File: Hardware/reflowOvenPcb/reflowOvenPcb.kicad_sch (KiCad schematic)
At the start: 0 parts

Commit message: PCB: started to add components
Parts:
- added U1: ATmega328P-A, Package_QFP:TQFP-32_7x7mm_P0.8mm, symbol MCU_Microchip_ATmega:ATmega328P-A
- added U2: MAX31856, Package_SO:TSSOP-14_4.4x5mm_P0.65mm, symbol Sensor_Temperature:MAX31856
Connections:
- new net: U1.21 (GND), U1.3 (GND), U1.5 (GND)
- new net: U1.4 (VCC), U1.6 (VCC)
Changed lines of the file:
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@@
 (kicad_sch (version 20230121) (generator eeschema)
   (paper "A4")
+  (symbol (lib_id "MCU_Microchip_ATmega:ATmega328P-A") (at 124.46 76.2 0) (unit 1)
+    (in_bom yes) (on_board yes) (dnp no) (fields_autoplaced)
+    (property "Reference" "U1" (at 126.4159 114.3 0)
+      (effects (font (size 1.27 1.27)) (justify left))
+    )
+    (property "Value" "ATmega328P-A" (at 126.4159 116.84 0)
+      (effects (font (size 1.27 1.27)) (justify left))
+    )
+    (property "Footprint" "Package_QFP:TQFP-32_7x7mm_P0.8mm" (at 124.46 76.2 0)
+      (effects (font (size 1.27 1.27) italic) hide)
+    )
+    (property "Datasheet" "http://ww1.microchip.com/downloads/en/DeviceDoc/ATmega328_P%20AVR%20MCU%20with%20picoPower%20Technology%20Data%20Sheet%2040001984A.pdf" (at 124.46 76.2 0)
+      (effects (font (size 1.27 1.27)) hide)
+    )
+    (pin "1")
+    (pin "10")
+    (pin "11")
+    (pin "12")
+    (pin "13")
+    (pin "14")
+    (pin "15")
+    (pin "16")
+    (pin "17")
+    (pin "18")
+    (pin "19")
+    (pin "2")
+    (pin "20")
+    (pin "21")
+    (pin "22")
+    (pin "23")
+    (pin "24")
+    (pin "25")
+    (pin "26")
+    (pin "27")
+    (pin "28")
+    (pin "29")
+    (pin "3")
+    (pin "30")
+    (pin "31")
+    (pin "32")
+    (pin "4")
+    (pin "5")
+    (pin "6")
+    (pin "7")
+    (pin "8")
+    (pin "9")
+    (instances
+      (project "reflowOvenPcb"
+        (path "/725b5e94-aab9-4b38-b207-68bd972bbc88"
+          (reference "U1") (unit 1)
+        )
+      )
+    )
+  )
+  (symbol (lib_id "Sensor_Temperature:MAX31856") (at 172.72 78.74 0) (unit 1)
+    (in_bom yes) (on_board yes) (dnp no) (fields_autoplaced)
+    (property "Reference" "U2" (at 177.2159 60.96 0)
+      (effects (font (size 1.27 1.27)) (justify left))
+    )
+    (property "Value" "MAX31856" (at 177.2159 63.5 0)
+      (effects (font (size 1.27 1.27)) (justify left))
+    )
+    (property "Footprint" "Package_SO:TSSOP-14_4.4x5mm_P0.65mm" (at 176.53 92.71 0)
+      (effects (font (size 1.27 1.27)) (justify left) hide)
+    )
+    (property "Datasheet" "https://datasheets.maximintegrated.com/en/ds/MAX31856.pdf" (at 171.45 73.66 0)
+      (effects (font (size 1.27 1.27)) hide)
+    )
+    (pin "1")
+    (pin "10")
+    (pin "11")
+    (pin "12")
+    (pin "13")
+    (pin "14")
+    (pin "2")
+    (pin "3")
+    (pin "4")
+    (pin "5")
+    (pin "6")
+    (pin "7")
+    (pin "8")
+    (pin "9")
+    (instances
+      (project "reflowOvenPcb"
+        (path "/725b5e94-aab9-4b38-b207-68bd972bbc88"
+          (reference "U2") (unit 1)
+        )
+      )
+    )
+  )
   (sheet_instances
     (path "/" (page "1"))

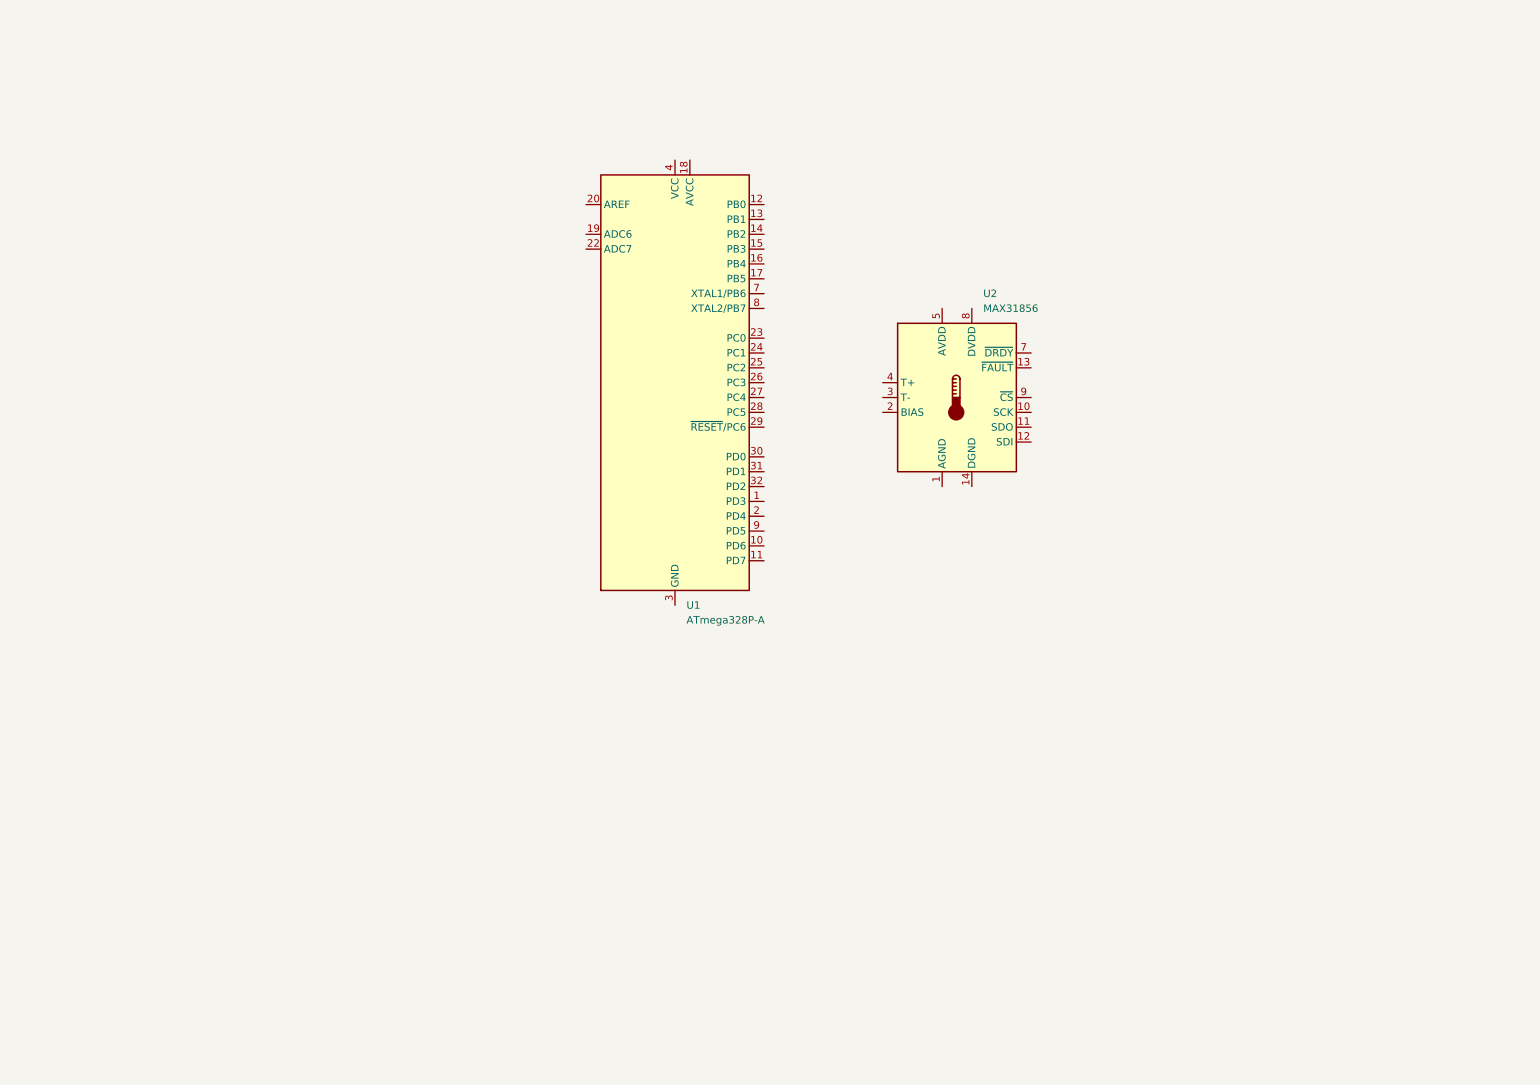
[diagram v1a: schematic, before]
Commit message: MCU wiring finished, added components to OLED SSD
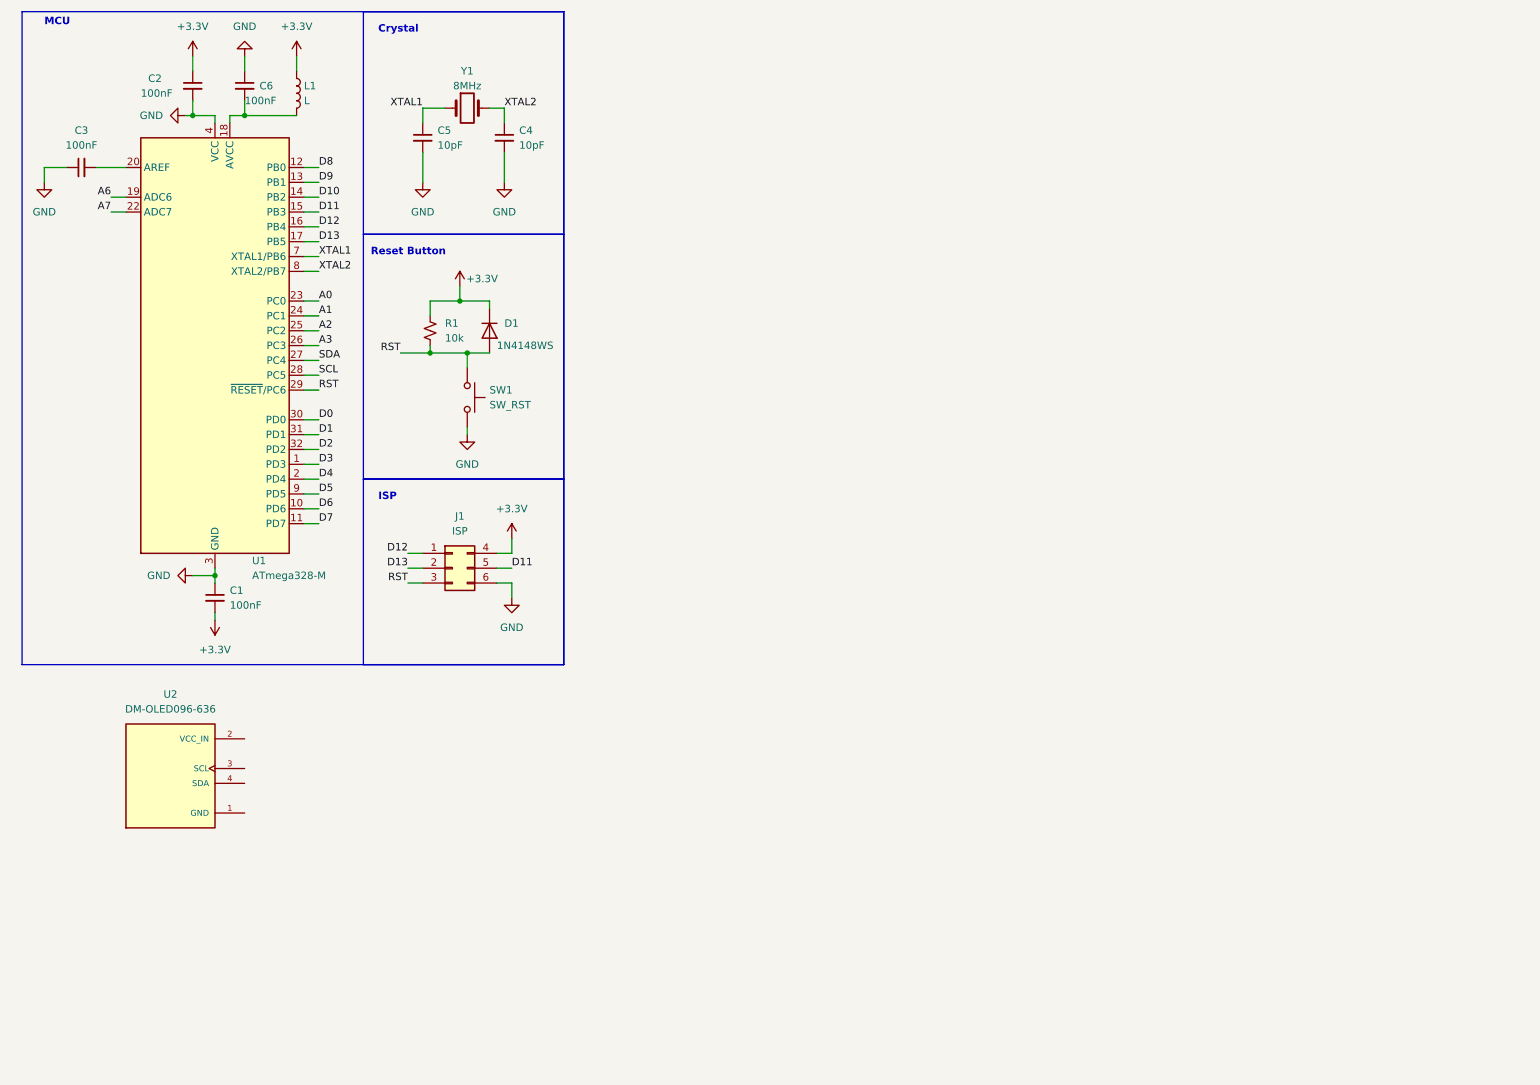
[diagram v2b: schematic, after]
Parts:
- removed U1: ATmega328P-A, Package_QFP:TQFP-32_7x7mm_P0.8mm, symbol MCU_Microchip_ATmega:ATmega328P-A
- removed U2: MAX31856, Package_SO:TSSOP-14_4.4x5mm_P0.65mm, symbol Sensor_Temperature:MAX31856
- added C1, C2, C3, C6: 100nF, symbol Device:C_Small
- added C4, C5: 10pF, symbol Device:C_Small
- added D1: 1N4148WS, Diode_SMD:D_SOD-323, symbol Diode:1N4148WS
- added J1: ISP, Connector_PinHeader_1.00mm:PinHeader_2x03_P1.00mm_Vertical_SMD, symbol Connector_Generic:Conn_02x03_Top_Bottom
- added L1: L, symbol Device:L
- added R1: 10k, symbol Device:R_Small_US
- added SW1: SW_RST, symbol Switch:SW_Push
- added U1: ATmega328-M, Package_DFN_QFN:QFN-32-1EP_5x5mm_P0.5mm_EP3.1x3.1mm, symbol MCU_Microchip_ATmega:ATmega328-M
- added U2: DM-OLED096-636, OLED_SSD1306:MODULE_DM-OLED096-636, symbol OLED_SSD1306:DM-OLED096-636
- added Y1: 8MHz, symbol Device:Crystal
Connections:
- new net: C6.2, L1.2, U1.18 (AVCC)
- new net: C3.2, U1.20 (AREF)
- new net +3.3V: C1.2, C2.1, D1.1 (K), J1.4 (Pin_4), L1.1, R1.1
- new net A0: U1.23 (PC0)
- new net A1: U1.24 (PC1)
- new net A2: U1.25 (PC2)
- new net A3: U1.26 (PC3)
- new net A6: U1.19 (ADC6)
- new net A7: U1.22 (ADC7)
- new net D0: U1.30 (PD0)
- new net D1: U1.31 (PD1)
- new net D10: U1.14 (PB2)
- new net D11: J1.5 (Pin_5), U1.15 (PB3)
- new net D12: J1.1 (Pin_1), U1.16 (PB4)
- new net D13: J1.2 (Pin_2), U1.17 (PB5)
- new net D2: U1.32 (PD2)
- new net D3: U1.1 (PD3)
- new net D4: U1.2 (PD4)
- new net D5: U1.9 (PD5)
- new net D6: U1.10 (PD6)
- new net D7: U1.11 (PD7)
- new net D8: U1.12 (PB0)
- new net D9: U1.13 (PB1)
- new net GND: C1.1, C2.2, C3.1, C4.2, C5.2, C6.1, J1.6 (Pin_6), SW1.2, U1.21 (GND), U1.3 (GND), U1.33 (GND), U1.4 (VCC), U1.5 (GND), U1.6 (VCC)
- new net RST: D1.2 (A), J1.3 (Pin_3), R1.2, SW1.1, U1.29 (~{RESET}/PC6)
- new net SCL: U1.28 (PC5)
- new net SDA: U1.27 (PC4)
- new net XTAL1: C5.1, U1.7 (XTAL1/PB6), Y1.1
- new net XTAL2: C4.1, U1.8 (XTAL2/PB7), Y1.2
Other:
- note added: "Crystal"
- note added: "ISP"
- note added: "MCU"
- note added: "Reset Button"
- company: (none) -> Designed By Alfonso Pinzon At Huskies lab
- title: (none) -> Reflow Oven PCB

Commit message: PCB EE: added ssr, fan and buzzer modulo
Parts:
- added BZ1: Buzzer, symbol Device:Buzzer
- added D2: LED, symbol Device:LED
- added J2: Fan_output, symbol Connector:Screw_Terminal_01x02
- added J4: SSR_Output, symbol Connector:Screw_Terminal_01x02
- added Q1, Q2, Q3: 2N3904, Package_TO_SOT_THT:TO-92_Inline, symbol Transistor_BJT:2N3904
- added R2, R3, R4: 2k2, symbol Device:R_Small_US
- added R5: 53k6, symbol Device:R_Small_US
- added R6: 53k5, symbol Device:R_Small_US
- added R7: 27k, symbol Device:R_Small_US
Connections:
- net +3.3V: now also U2.2 (VCC_IN), R2.2, R3.2
- net A0: now also R6.1
- net A1: now also R5.1
- net D4: now also R4.2
- net D5: now also R7.1
- net GND: now also U2.1 (GND), D2.1 (K), Q1.1 (E), Q2.1 (E), Q3.1 (E)
- net SCL: now also U2.3 (SCL), R2.1
- net SDA: now also U2.4 (SDA), R3.1
- new net: Q2.2 (B), R6.2
- new net: Q1.2 (B), R5.2
- new net: J2.2 (Pin_2), Q1.3 (C)
- new net: J4.2 (Pin_2), Q2.3 (C)
- new net: D2.2 (A), R4.1
- new net: Q3.2 (B), R7.2
- new net: BZ1.2 (+), Q3.3 (C)
- new net +5V: BZ1.1 (-), J2.1 (Pin_1), J4.1 (Pin_1)
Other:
- note added: "BUZZER"
- note added: "Fan"
- note added: "Oled LCD Screen"
- note added: "SSR"
- note added: "Status LED"
- moved on the sheet: U2
